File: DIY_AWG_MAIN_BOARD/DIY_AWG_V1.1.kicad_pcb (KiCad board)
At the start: 4 copper layers, 224.5 x 101 mm, 268 parts, among them CN1 RH-5019, CN10 RH-5019, CN11 RH-5019, CN12 RH-5019, CN2 RH-5019, CN3 RH-5019, CN4 RH-5019, CN5 RH-5019, CN6 RH-5019, CN7 RH-5019, CN8 RH-5019, CN9 RH-5019, IC1 TLV3544IPWR, IC2 ADG704BRMZ-REEL7, IC3 LMH6505MAX, IC4 THS3091DDAR, J1 Conn_01x04_Socket, J2 Conn_01x04_Pin, J3 Conn_01x02_Pin, SW1 SW_Push, SW10 SW_Push, SW11 SW_Push, SW12 SW_Push, SW13 SW_Push, SW14 SW_Push, SW15 SW_Push, SW16 SW_Push, SW17 SW_Push, SW18 SW_Push, SW19 SW_Push, SW2 SW_Push, SW20 SW_Push, SW21 SW_Push, SW22 SW_Push, SW23 SW_Push, SW24 SW_Push, SW25 SW_Push, SW3 SW_Push, SW4 SW_Push, SW5 SW_Push, SW6 SW_Push, SW7 SW_Push, SW8 SW_Push, SW9 SW_Push, U1 AMS1117-3.3, U10 STM32G473VETx, U11 8121H-50.000NK33DRL, U12 AD9834, U13 OPA2171AIDR, U14 EC12D1564402, U15 EC12E2430404, U2 ADP7118ARDZ-3.3-R7, U3 ADP7118ARDZ-3.3-R7, U4 TPS7A3301RGWR, U5 TPS7A4701RGWR, U6 TPS7A3301RGWR, U7 TPS7A4701RGWR, U8 USBLC6-2SC6, U9 161N-4BVS11, X1 SX2M8.000B10F20TNN

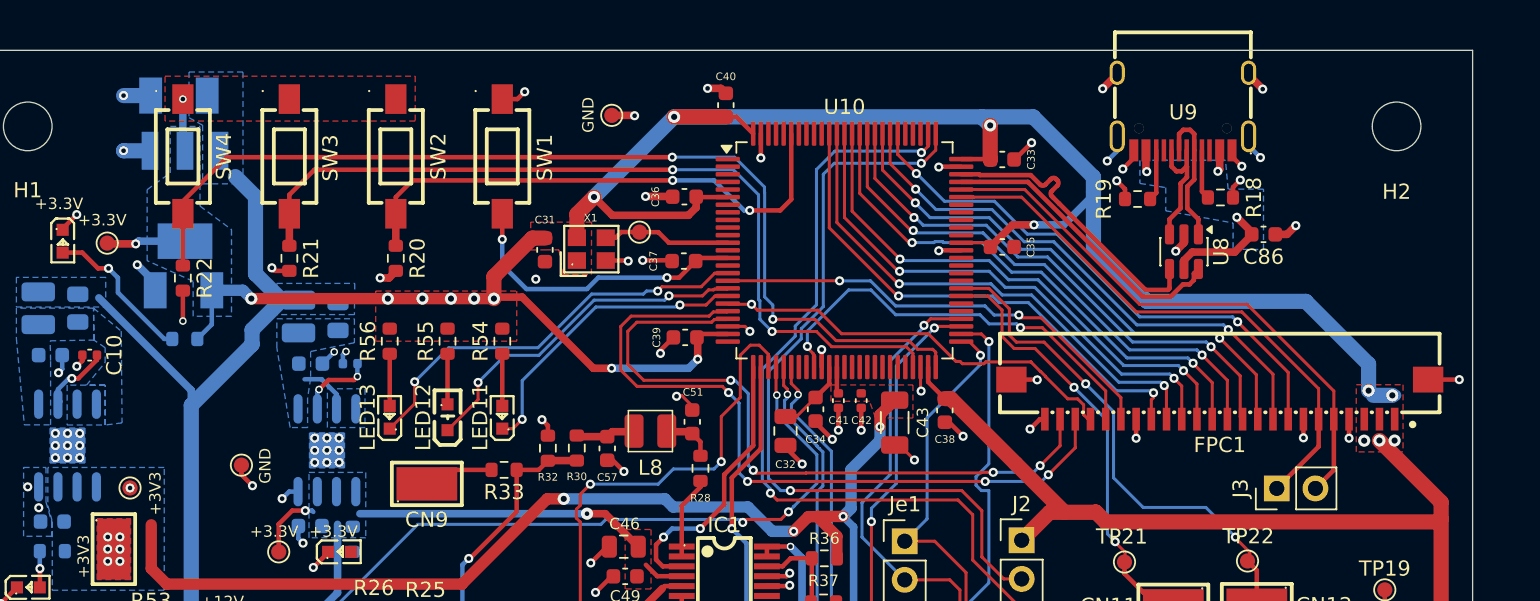
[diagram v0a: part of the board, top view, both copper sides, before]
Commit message: Updated main PCB, daughter PCB
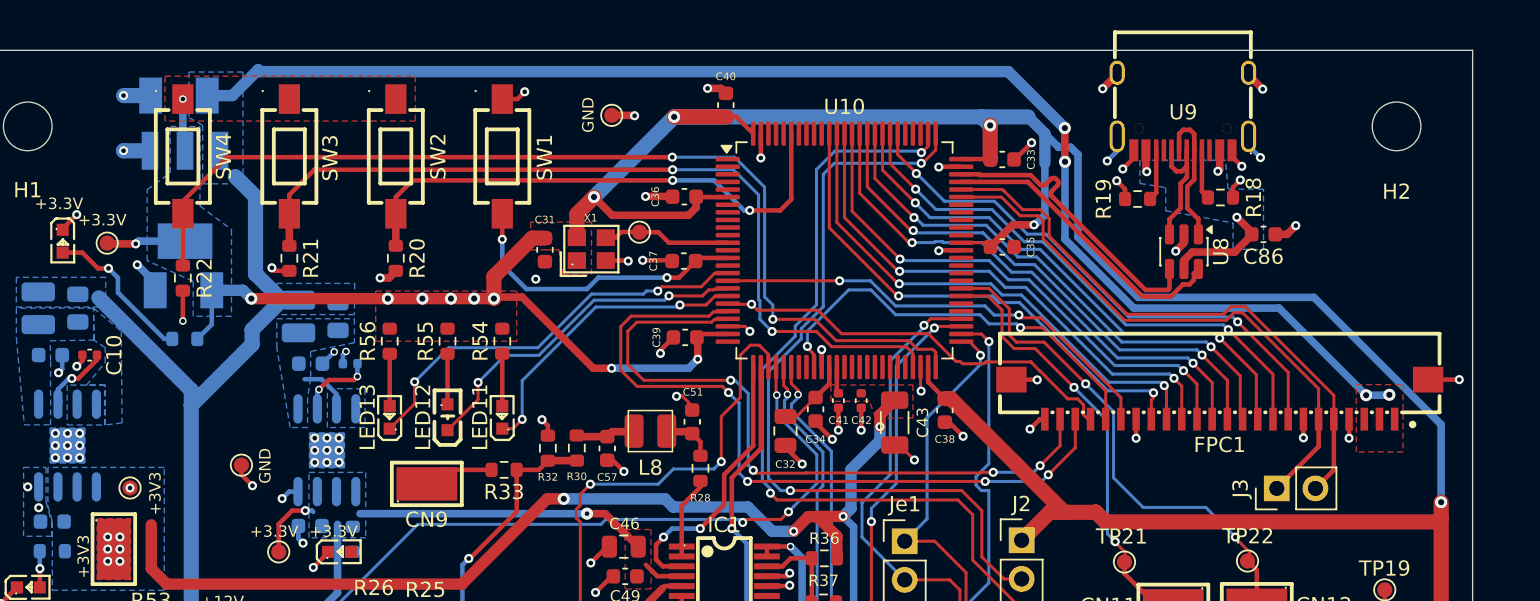
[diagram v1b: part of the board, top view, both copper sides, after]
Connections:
- FPC1 pad 1: +3V3 -> +VSW5V0
- FPC1 pad 2: +3V3 -> +VSW5V0
- FPC1 pad 3: +3V3 -> +VSW5V0
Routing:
- net +VSW5V0: track 110.4 -> 202.0 mm, vias 2 -> 6
- net +3V3: track 230.4 -> 234.4 mm, vias 21 -> 17
- net /STM32_MCU/UART_TX4: track 36.4 -> 37.5 mm
- net /STM32_MCU/UART_RX4: track 36.9 -> 37.8 mm
- added copper zone on F.Cu, net +VSW5V0

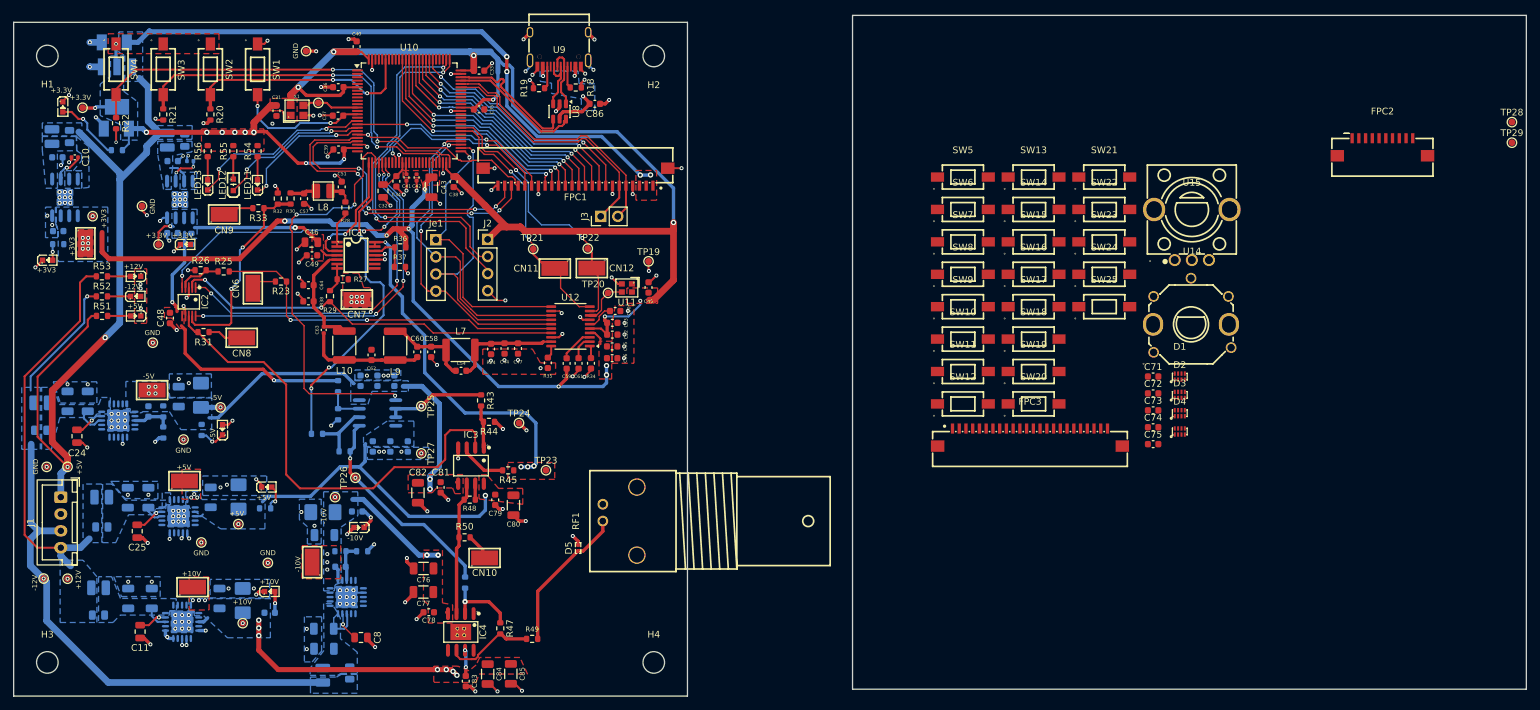
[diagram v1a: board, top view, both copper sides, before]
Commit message: Updated daughter board and main board PCB design schematics
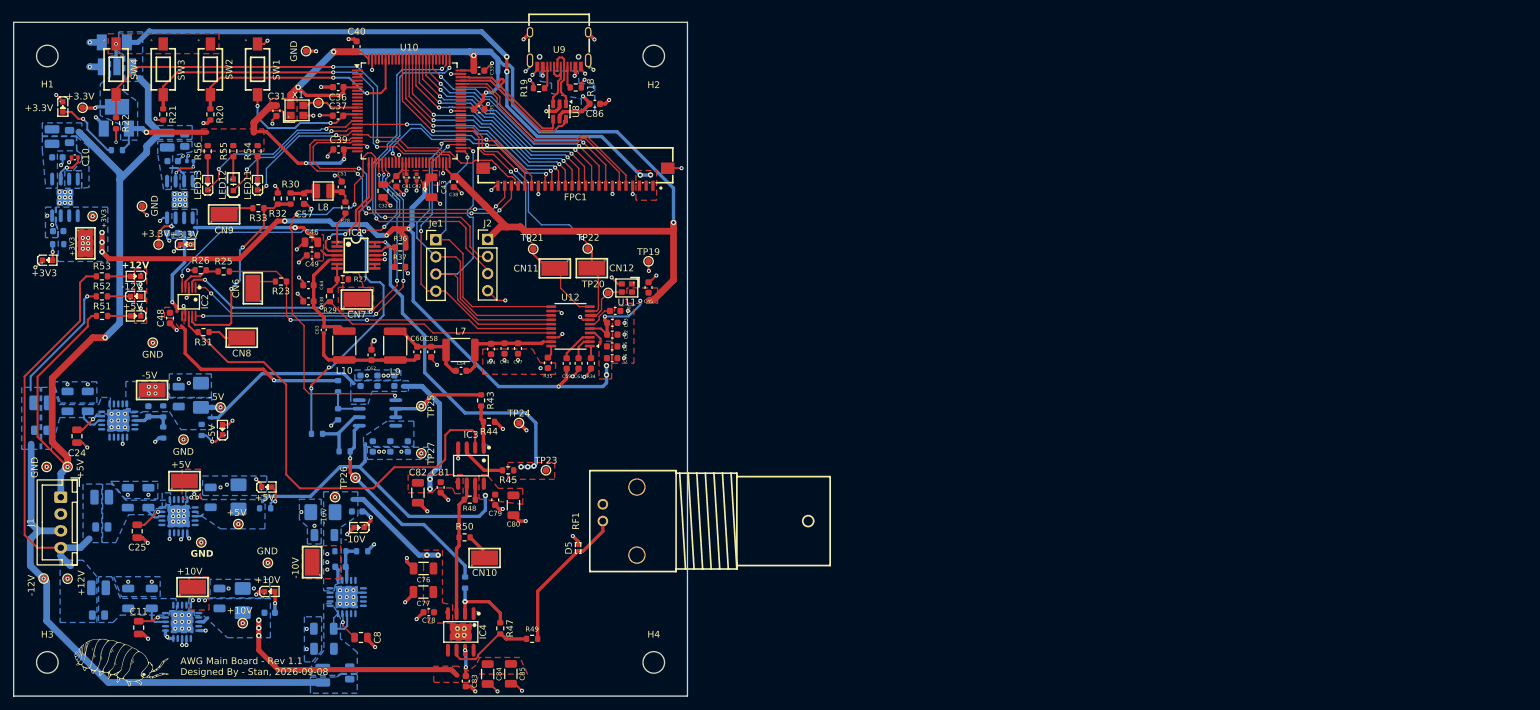
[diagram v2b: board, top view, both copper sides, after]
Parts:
- removed C71, C72, C73, C74, C75: 100n, Capacitor_SMD:C_0603_1608Metric
- removed D1, D2, D3, D4: RL20108Q0332LC, easyeda2kicad:DFN-8_L2.0-W1.0-P0.50-BL
- removed FPC2: XW1020012-100R-002, easyeda2kicad:FPC-SMD_10P-P1.00_XW1020012-100R-001
- removed FPC3: FC-10A24P11H20, easyeda2kicad:FPC-SMD_24P-P1.00_FC-10A24P11H20
- removed J3: Conn_01x02_Pin, Connector_PinHeader_2.54mm:PinHeader_1x02_P2.54mm_Vertical
- removed SW10, SW11, SW12, SW13, SW14, SW15, SW16, SW17, SW18, SW19, SW20, SW21, SW22, SW23, SW24, SW25, SW5, SW6, SW7, SW8, SW9: SW_Push, easyeda2kicad:SW-SMD_L6.1-W3.5-LS8.6
- removed TP28, TP29: TestPoint, TestPoint:TestPoint_Pad_D1.0mm
- removed U14: EC12D1564402, easyeda2kicad:SW-TH_EC12D1564402
- removed U15: EC12E2430404, easyeda2kicad:SW-TH_ALPSALPINE_EC12EXXXX
- added G***: LOGO, LOGO, F.Cu at (36.9, 117.7)
- moved C11 0.63 mm to (39.6, 112.9)
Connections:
- IC4 pad : (no net) -> GND
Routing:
- net +3V3: track 234.4 -> 227.1 mm, vias 17 -> 12
- net /STM32_MCU/UART_TX4: track 37.5 -> 31.8 mm
- net GND: track 172.1 -> 177.5 mm, vias 206 -> 208
- net /STM32_MCU/UART_RX4: track 37.8 -> 32.8 mm
- net +VSW5V0: track 202.0 -> 203.0 mm
- net Net-(IC1C-INC-): track 0.00 -> 0.65 mm
- net /AD9834_DDS/SPI2_MOSI: track 46.1 -> 46.4 mm, vias 2 -> 1
- net /STM32_MCU/ENC1_A: track 27.5 -> 27.8 mm, vias 1 -> 0
- net Net-(LED2-A): vias 0 -> 1
- net Net-(CN7-Pad1): vias 6 -> 0
- net +3.3VA_2: vias 14 -> 17
- net +10.0VA: vias 13 -> 9
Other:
- board size 224.5 x 101 mm -> 100 x 100 mm
- board text added: "AWG Main Board - Rev 1.1 Designed By - Stan, 2026-09-08"

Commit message: Updated main and daughter board PCB design
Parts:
- moved RF1 5.99 mm to (111.0, 91.1)
- moved D5 5.64 mm to (104.8, 95.4)
- moved LED10 1.03 mm to (38.1, 60.7)
- moved LED8 1.03 mm to (38.1, 66.6)
- moved LED9 1.03 mm to (38.1, 63.7)
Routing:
- net /Amplifier/SIG_OUT: track 21.9 -> 27.9 mm
- net +3V3: track 227.1 -> 229.2 mm
- net GND: track 177.5 -> 176.0 mm
- net Net-(LED9-K): track 3.43 -> 2.40 mm
- net Net-(LED10-A): track 3.43 -> 2.40 mm
- net Net-(LED8-A): track 3.42 -> 2.40 mm
- net -5.0VA: vias 7 -> 6
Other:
- board text added: "50M"
- board text added: "8M"
- board text added: "FSEL"
- board text added: "GAIN"
- board text added: "MUX_OUT"
- board text added: "OFFSET"
- board text added: "PSEL"
- board text added: "REF"
- board text added: "SQUARE"
- board text added: "VGA_OUT"
- board text added: "VOUT"
- board text added: "WAVE1"

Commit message: Updated main PCB design
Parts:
- moved R50 1.11 mm to (87.9, 98.3), turned to 90 degrees
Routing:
- net Net-(CN10-Pad1): track 3.95 -> 6.25 mm
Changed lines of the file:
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@@
 			(plot_on_all_layers_selection 0x00000000_00000000_00000000_00000000)
 			(disableapertmacros no)
-			(usegerberextensions no)
-			(usegerberattributes yes)
-			(usegerberadvancedattributes yes)
-			(creategerberjobfile yes)
+			(usegerberextensions yes)
+			(usegerberattributes no)
+			(usegerberadvancedattributes no)
+			(creategerberjobfile no)
 			(dashed_line_dash_ratio 12)
 			(dashed_line_gap_ratio 3)
@@
 			(outputformat 1)
 			(mirror no)
-			(drillshape 1)
+			(drillshape 0)
 			(scaleselection 1)
-			(outputdirectory "")
+			(outputdirectory "../../../../../Downloads/")
 		)
 	)
@@
 	(footprint "Resistor_SMD:R_0603_1608Metric"
 		(layer "F.Cu")
-		(at 87.92 99.46 180)
+		(at 87.94 98.35 90)
 		(descr "Resistor SMD 0603 (1608 Metric), square (rectangular) end terminal, IPC-7351 nominal, (Body size source: IPC-SM-782 page 72, https://www.pcb-3d.com/wordpress/wp-content/uploads/ipc-sm-782a_amendment_1_and_2.pdf)")
 		(tags "resistor")
 		(property "Reference" "R50"
-			(at 0 1.6 0)
+			(at 0 1.6 90)
 			(layer "F.SilkS")
 			(effects
@@
 		)
 		(property "Value" "0"
-			(at 0 1.43 0)
+			(at 0 1.43 90)
 			(layer "F.Fab")
 			(effects
@@
 		)
 		(property "Datasheet" "https://www.lcsc.com/datasheet/C2596815.pdf?spm=wm.sxq.inf.ggs___wm.fly.bg.0.xh&lcsc_vid=EVldUV1eRAJaUwYHFAdaVVJVQFRYUFFWFAdfXgVUElQxVlNeQlNcUlJeRFdcVjsOAxUeFF5JWBYZEEoKFBINSQcJGk4%3D"
-			(at 0 0 0)
+			(at 0 0 90)
 			(layer "F.Fab")
 			(hide yes)
@@
 		)
 		(property "Description" "Resistor"
-			(at 0 0 0)
+			(at 0 0 90)
 			(layer "F.Fab")
 			(hide yes)
@@
 		)
 		(property "Component Name" "RK73Z1JRTTD"
-			(at 0 0 180)
+			(at 0 0 90)
 			(unlocked yes)
 			(layer "F.Fab")
@@
 		)
 		(property "LCSC ID" "C2596815"
-			(at 0 0 180)
+			(at 0 0 90)
 			(unlocked yes)
 			(layer "F.Fab")
@@
 		(duplicate_pad_numbers_are_jumpers no)
 		(fp_line
-			(start -0.237258 0.5225)
-			(end 0.237258 0.5225)
+			(start -0.237258 -0.5225)
+			(end 0.237258 -0.5225)
 			(stroke
 				(width 0.12)
@@
 		)
 		(fp_line
-			(start -0.237258 -0.5225)
-			(end 0.237258 -0.5225)
+			(start -0.237258 0.5225)
+			(end 0.237258 0.5225)
 			(stroke
 				(width 0.12)
@@
 		)
 		(fp_text user "${REFERENCE}"
-			(at 0 0 0)
+			(at 0 0 90)
 			(layer "F.Fab")
 			(effects
@@
 		)
 		(pad "1" smd roundrect
-			(at -0.825 0 180)
+			(at -0.825 0 90)
 			(size 0.8 0.95)
 			(layers "F.Cu" "F.Mask" "F.Paste")
@@
 		)
 		(pad "2" smd roundrect
-			(at 0.825 0 180)
+			(at 0.825 0 90)
 			(size 0.8 0.95)
 			(layers "F.Cu" "F.Mask" "F.Paste")
@@
 	)
 	(segment
-		(start 87.1 97.75)
-		(end 87.1 97.96)
-		(width 0.5)
-		(layer "F.Cu")
-		(net "/Amplifier/VGA1_OUT")
-	)
-	(segment
-		(start 86.73 101.09)
-		(end 86.73 110.78)
-		(width 0.5)
-		(layer "F.Cu")
-		(net "/Amplifier/VGA1_OUT")
-	)
-	(segment
-		(start 87.11 97.74)
-		(end 87.1 97.75)
-		(width 0.5)
-		(layer "F.Cu")
-		(net "/Amplifier/VGA1_OUT")
-	)
-	(segment
 		(start 88.24 93.495)
 		(end 87.865 93.87)
@@
 	)
 	(segment
-		(start 87.865 93.87)
-		(end 87.11 94.625)
-		(width 0.5)
-		(layer "F.Cu")
-		(net "/Amplifier/VGA1_OUT")
-	)
-	(segment
 		(start 88.24 91.5)
 		(end 88.24 93.495)
@@
 	)
 	(segment
-		(start 87.11 94.625)
-		(end 87.11 97.74)
+		(start 87.94 97.525)
+		(end 87.94 93.945)
 		(width 0.5)
 		(layer "F.Cu")
@@
 	)
 	(segment
-		(start 87.1 97.96)
-		(end 87.095 97.965)
-		(width 0.5)
-		(layer "F.Cu")
-		(net "/Amplifier/VGA1_OUT")
-	)
-	(segment
-		(start 87.095 100.725)
-		(end 86.73 101.09)
+		(start 86.73 98.735)
+		(end 86.73 110.78)
 		(width 0.5)
 		(layer "F.Cu")
@@
 	)
 	(segment
-		(start 87.095 97.965)
-		(end 87.095 99.46)
+		(start 87.94 93.945)
+		(end 87.865 93.87)
 		(width 0.5)
 		(layer "F.Cu")
@@
 	)
 	(segment
-		(start 87.095 99.46)
-		(end 87.095 100.725)
+		(start 87.94 97.525)
+		(end 86.73 98.735)
 		(width 0.5)
 		(layer "F.Cu")
@@
 	)
 	(segment
-		(start 88.745 99.46)
-		(end 90.61 101.325)
+		(start 87.94 100.2)
+		(end 90.26 102.52)
+		(width 0.5)
+		(layer "F.Cu")
+		(net "Net-(CN10-Pad1)")
+	)
+	(segment
+		(start 90.26 102.52)
+		(end 90.89 102.52)
+		(width 0.5)
+		(layer "F.Cu")
+		(net "Net-(CN10-Pad1)")
+	)
+	(segment
+		(start 87.94 99.175)
+		(end 87.94 100.2)
 		(width 0.5)
 		(layer "F.Cu")

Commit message: Updated main PCB design
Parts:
- moved C63 2.16 mm to (69.2, 68.5), turned to 180 degrees
- moved L10 1.80 mm to (69.2, 72.6), turned to 180 degrees
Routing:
- net /AD9834_DDS/VOUT: track 16.0 -> 19.3 mm
- net Net-(C60-Pad2): track 17.7 -> 14.8 mm
- net /AD9834_DDS/DAC1_OUT2: track 48.0 -> 50.0 mm

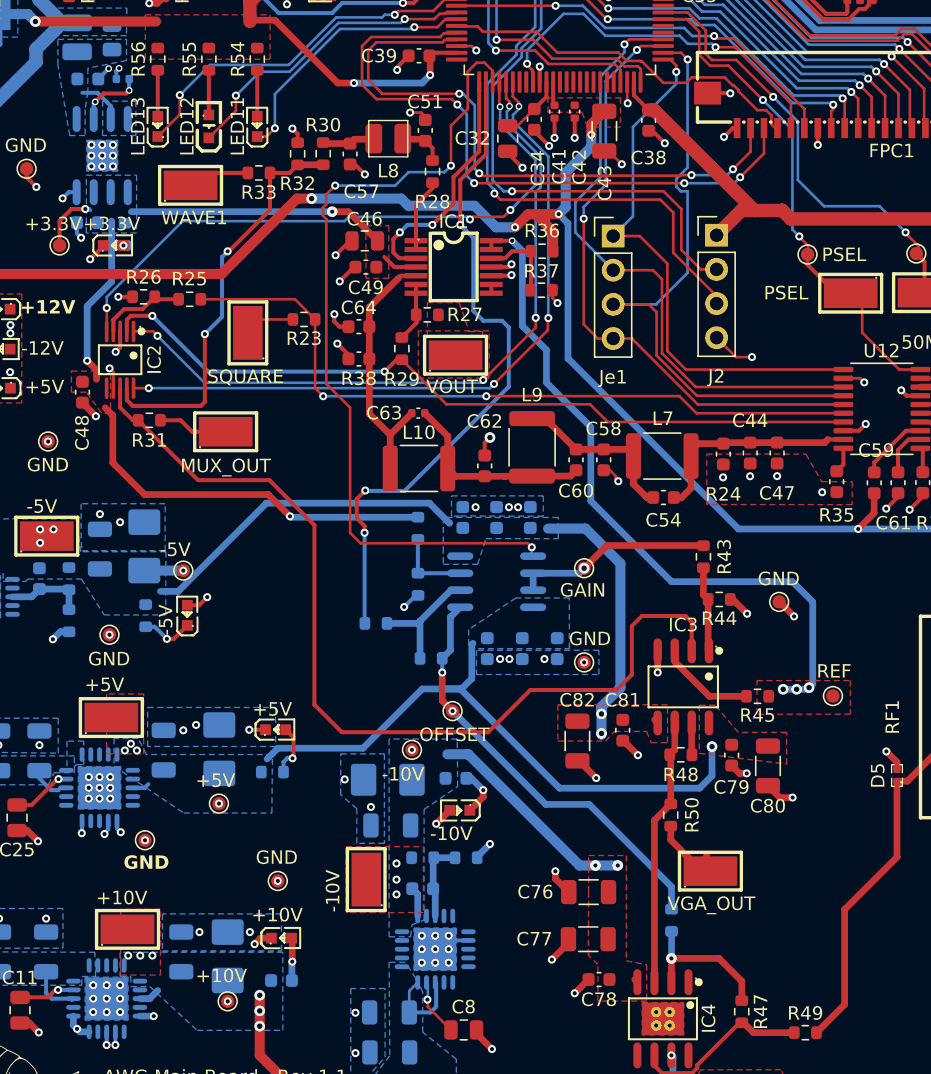
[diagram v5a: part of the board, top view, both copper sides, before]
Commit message: Updated main board schematic and design
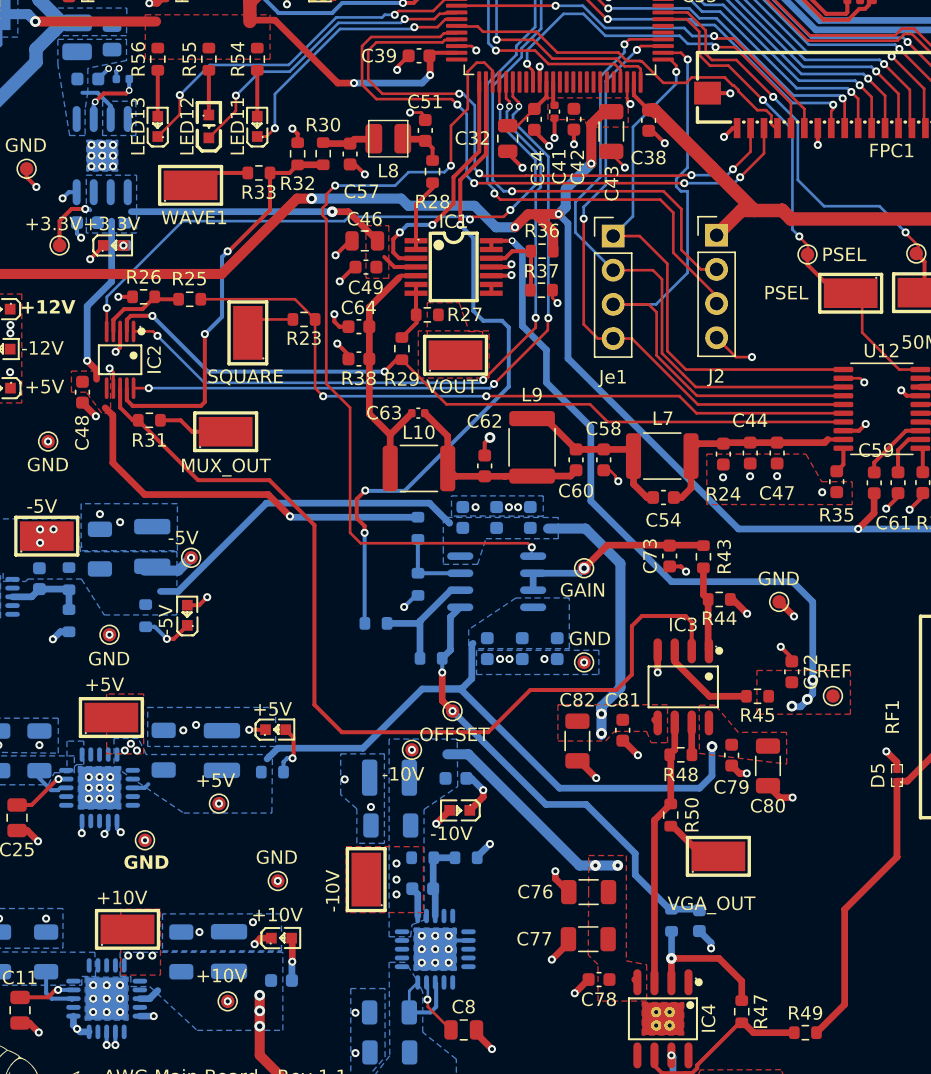
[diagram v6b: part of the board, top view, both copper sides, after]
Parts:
- added C71: 100n, Capacitor_SMD:C_0603_1608Metric, B.Cu at (90.1, 106.2)
- added C72: 100n, Capacitor_SMD:C_0603_1608Metric, F.Cu at (96.9, 87.7)
- added C73: 100n, Capacitor_SMD:C_0603_1608Metric, F.Cu at (87.9, 79.1)
- C17, C19, C28, C30: value 22u -> 100u; footprint easyeda2kicad:CAP-SMD_L3.5-W2.8-FD -> Capacitor_SMD:C_1210_3225Metric
- C42: value 4.7n -> 100n; footprint Capacitor_SMD:C_0402_1005Metric -> Capacitor_SMD:C_0603_1608Metric
- moved CN10 1.25 mm to (91.5, 101.4)
- moved TP15 1.12 mm to (52.3, 79.2)
- moved C30 0.59 mm to (49.4, 78.4)
- moved C42 0.56 mm to (80.7, 46.6)
- moved C43 0.52 mm to (83.5, 47.5)
- moved C17 0.36 mm to (55.1, 108.5)
- moved C28 0.22 mm to (54.6, 93.5)
- moved C19 0.20 mm to (67.0, 95.6)
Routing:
- net GND: track 176.0 -> 180.2 mm, vias 208 -> 211
- net Net-(CN10-Pad1): track 6.25 -> 3.09 mm
- net /AD9834_DDS/DC_OFFSET: track 32.0 -> 34.0 mm
- net -5.0VA: track 48.0 -> 48.9 mm
- net +3.3VA_2: track 120.3 -> 120.8 mm
